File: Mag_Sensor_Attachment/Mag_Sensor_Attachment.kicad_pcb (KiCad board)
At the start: 2 copper layers, 19.5 x 12.5 mm, 5 parts, among them J1 Conn_01x07_Socket, U1 MA730

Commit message: made cuter and added silkscreens
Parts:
- removed J1: Conn_01x07_Socket, Connector_Molex:Molex_Nano-Fit_105309-xx07_1x07_P2.50mm_Vertical
- added J2: Conn_01x06_Socket, Connector_Molex:Molex_Nano-Fit_105309-xx06_1x06_P2.50mm_Vertical, F.Cu at (168.0, 84.8)
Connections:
- U1 pad 16: /Mag_High -> unconnected-(U1-MGH-Pad16)
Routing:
- net /Mag_High: track 13.5 -> 0.00 mm, vias 2 -> 0
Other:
- board size 19.5 x 12.5 mm -> 17.1 x 12.5 mm
- board text added: "HALL_E_CONN"

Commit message: made bom
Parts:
- moved U1 4.03 mm to (168.5, 91.8)
- moved C1 2.26 mm to (173.8, 92.2)
- moved R3 1.37 mm to (176.9, 92.2)
- moved D1 0.53 mm to (180.0, 92.2)
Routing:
- net /MAG_CLK: track 16.3 -> 11.8 mm, vias 0 -> 2
- net /MGSLV_Input: track 11.2 -> 14.9 mm
- net /VDD: track 13.3 -> 15.4 mm
- net /MAGSLV_Output: track 13.7 -> 15.3 mm
- net /MAG_CS: track 10.5 -> 8.92 mm
- net Net-(D1-A): track 2.27 -> 3.12 mm
- net GND: track 4.71 -> 4.12 mm

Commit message: fixed review stuffs
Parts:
- removed J2: Conn_01x06_Socket, Connector_Molex:Molex_Nano-Fit_105309-xx06_1x06_P2.50mm_Vertical
- added J1: Conn_01x06_Socket, Connector_Molex:Molex_Nano-Fit_105309-xx06_1x06_P2.50mm_Vertical, F.Cu at (180.5, 84.8)
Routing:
- added copper zone on F.Cu, net GND
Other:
- board text added: "."
- board text added: "HALL_E CONN"
- board text removed: "HALL_E_CONN"

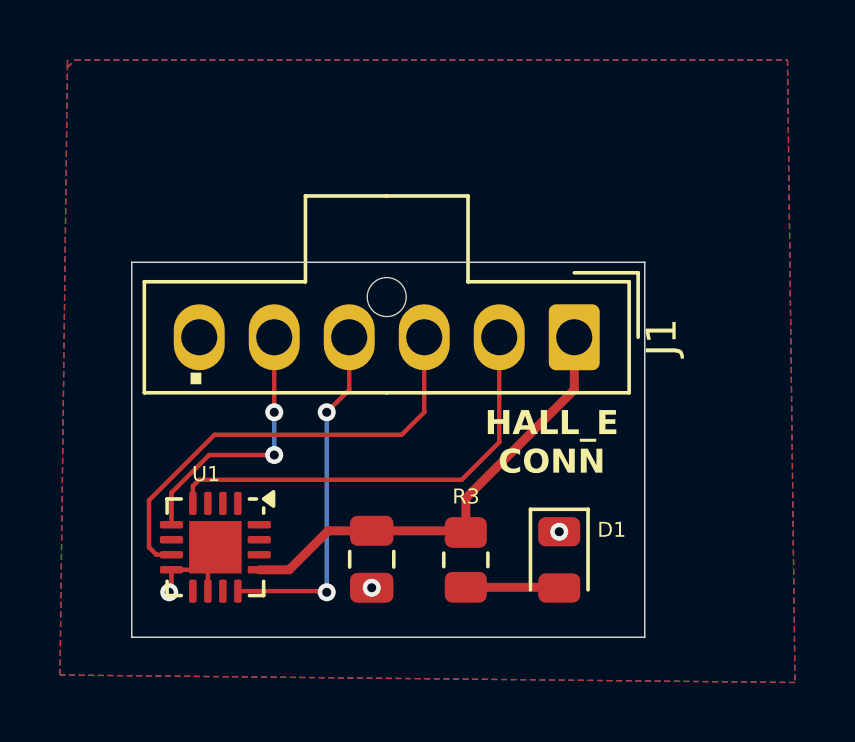
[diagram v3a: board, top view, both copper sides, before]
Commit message: fixed imu connector oops
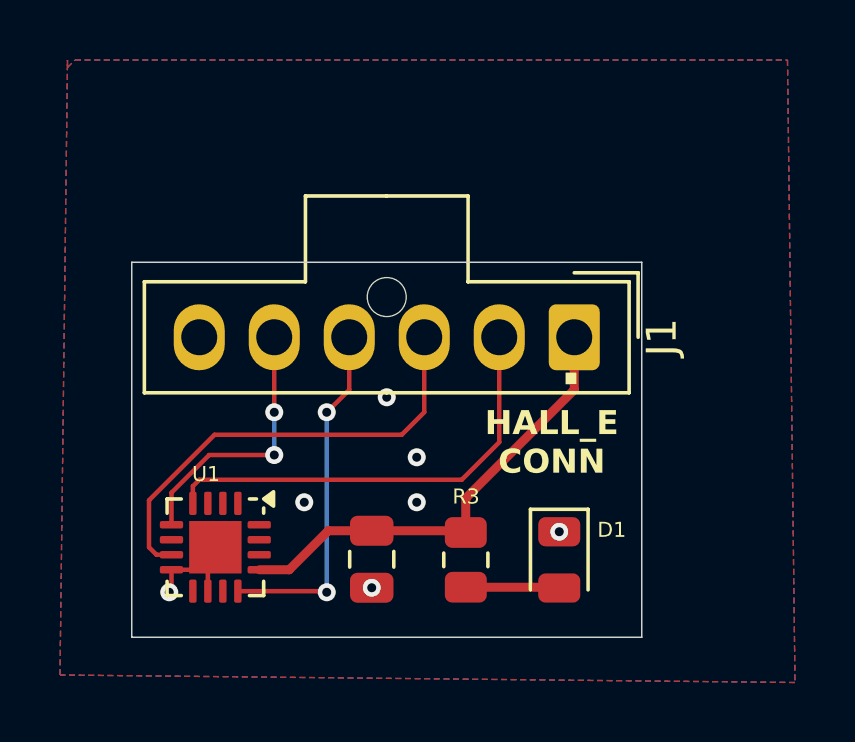
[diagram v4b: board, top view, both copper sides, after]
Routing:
- net GND: vias 3 -> 7
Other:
- board size 17.1 x 12.5 mm -> 17 x 12.5 mm
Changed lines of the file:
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@@
 		)
 		(fp_text user "${REFERENCE}"
-			(at 1.1 6.25 360)
+			(at 1.1 6.25 0)
 			(layer "F.Fab")
 			(effects
@@
 			(pintype "passive")
 		)
-		(model "${KICAD8_3DMODEL_DIR}/Connector_Molex.3dshapes/Molex_Nano-Fit_105309-xx06_1x06_P2.50mm_Vertical.wrl"
+		(model "${KIPRJMOD}/3Dmodels/1053091106.stp"
 			(offset
-				(xyz 0 0 0)
+				(xyz 0 -6.5 5)
 			)
 			(scale
@@
 			)
 			(rotate
-				(xyz 0 0 0)
+				(xyz 0 0 -90)
 			)
 		)
@@
 	(gr_rect
 		(start 165.75 82.25)
-		(end 182.85 94.75)
+		(end 182.75 94.75)
 		(stroke
 			(width 0.05)
@@
 	)
 	(gr_text "."
-		(at 167.5 86.5 0)
+		(at 180 86.5 0)
 		(layer "F.SilkS")
 		(effects
@@
 	)
 	(via
+		(at 171.5 90.25)
+		(size 0.6)
+		(drill 0.3)
+		(layers "F.Cu" "B.Cu")
+		(free yes)
+		(net 1)
+	)
+	(via
 		(at 173.75 93.1)
 		(size 0.6)
 		(drill 0.3)
 		(layers "F.Cu" "B.Cu")
+		(net 1)
+	)
+	(via
+		(at 175.25 90.25)
+		(size 0.6)
+		(drill 0.3)
+		(layers "F.Cu" "B.Cu")
+		(free yes)
+		(net 1)
+	)
+	(via
+		(at 175.25 88.75)
+		(size 0.6)
+		(drill 0.3)
+		(layers "F.Cu" "B.Cu")
+		(free yes)
+		(net 1)
+	)
+	(via
+		(at 174.25 86.75)
+		(size 0.6)
+		(drill 0.3)
+		(layers "F.Cu" "B.Cu")
+		(free yes)
 		(net 1)
 	)
@@
 		(hatch edge 0.5)
 		(connect_pads
-			(clearance 0.5)
-		)
-		(min_thickness 0.25)
+			(clearance 0.3)
+		)
+		(min_thickness 0.15)
 		(filled_areas_thickness no)
 		(fill yes
-			(thermal_gap 0.5)
-			(thermal_bridge_width 0.5)
+			(thermal_gap 0.4)
+			(thermal_bridge_width 0.25)
 		)
 		(polygon
